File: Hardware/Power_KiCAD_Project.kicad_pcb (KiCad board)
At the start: 4 copper layers, 80 x 93.2 mm, 83 parts, among them J1 Barrel_Jack_MountingPin, J2 XT60 Cell 5, J3 XT60 Cell 4, J4 XT60 Cell 3, J5 XT60 Cell 2, J6 XT60 Cell 1, J7 XT60 To External Switch, J8 L717SDC37P1ACH4F, Q1 PSMN2R6-40YS, Q2 BSS84PH6327XTSA2, Q3 PSMN2R6-40YS, SW1 Reboot, U1 MCP9808_MSOP, U2 MCP9808_MSOP, U3 LM2678SX-5.0/NOPB, U4 LM2678SX-3.3/NOPB, U5 BQ76920PW, U6 STM32L562VET, Y1 32MHz

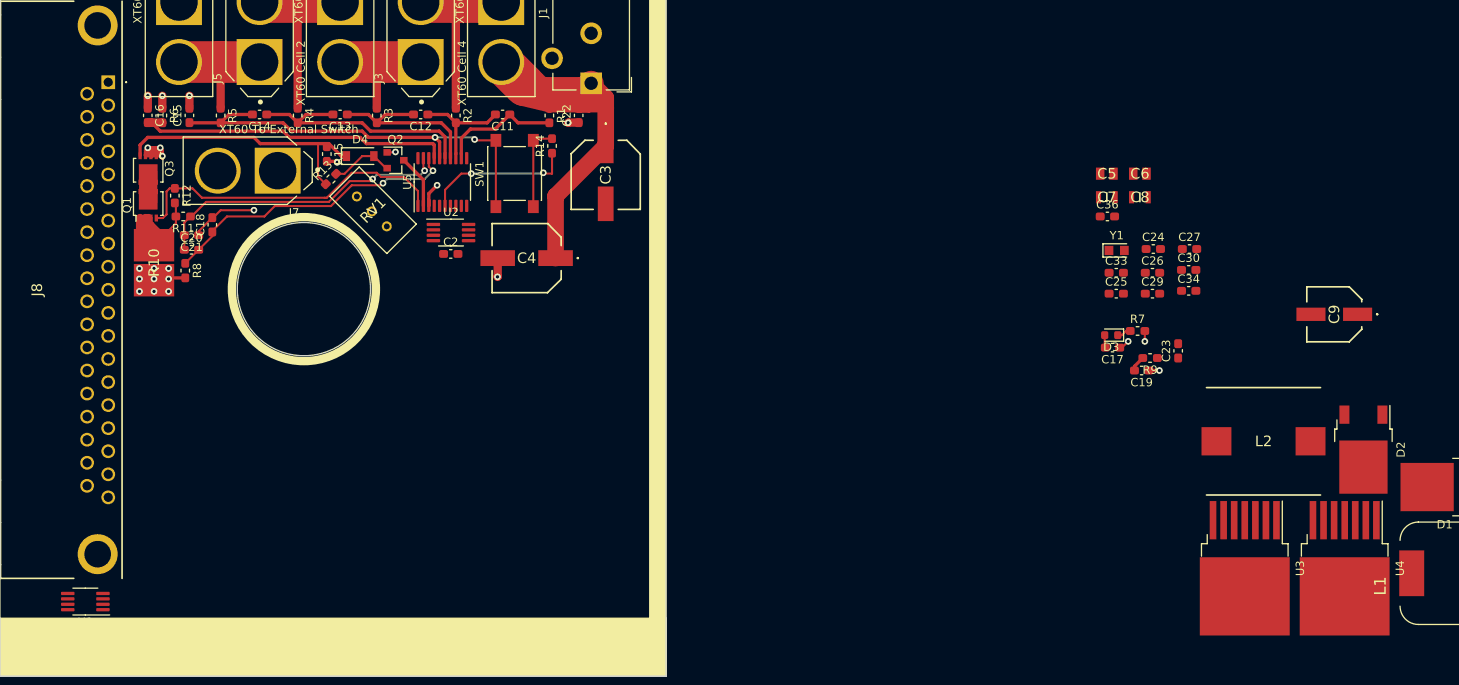
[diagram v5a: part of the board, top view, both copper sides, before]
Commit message: Routed 3v3 and 5v buck converters
Switched to working on my laptop so some of the component references might be messed up for a bit
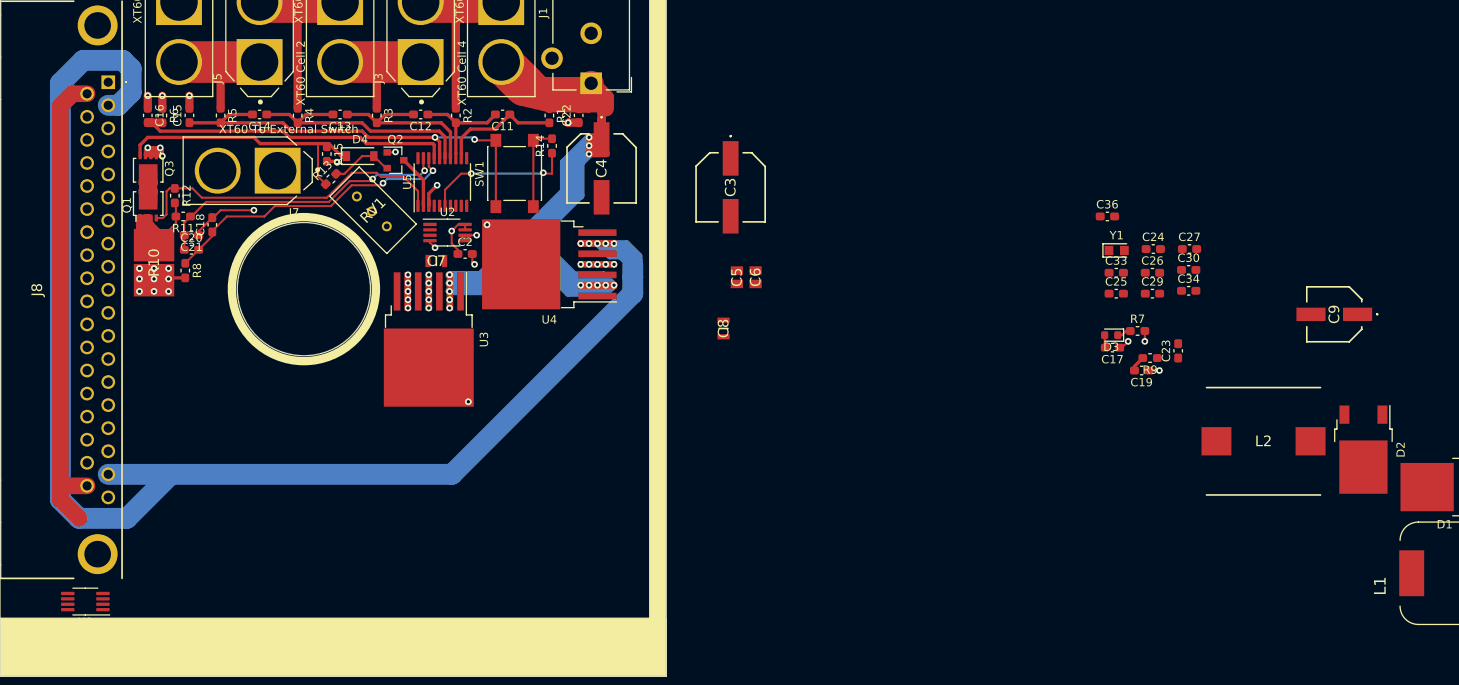
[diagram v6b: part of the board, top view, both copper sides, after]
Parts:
- moved U4 102.3 mm to (146.0, 95.5), turned to 180 degrees
- moved U3 101.8 mm to (131.5, 104.5)
- moved C7 80.9 mm to (132.4, 95.1)
- moved C8 52.4 mm to (166.9, 103.2), turned to 270 degrees
- moved C6 47.8 mm to (170.8, 97.0), turned to 270 degrees
- moved C5 46.1 mm to (168.5, 97.0), turned to 270 degrees
- moved C3 15.1 mm to (167.8, 86.2)
- moved C4 14.0 mm to (152.2, 84.0), turned to 270 degrees
- moved C2 1.73 mm to (135.9, 94.2)
- moved U2 0.42 mm to (133.8, 91.7)
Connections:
- U3 pad 8: (no net) -> GND
- U4 pad 8: (no net) -> GND
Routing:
- net +3V3: track 0.00 -> 190.1 mm, vias 0 -> 6
- net /PACK_M5: track 65.4 -> 182.4 mm, vias 0 -> 13
- net +5V: track 0.00 -> 57.7 mm, vias 0 -> 5
- net GND: track 2.26 -> 4.50 mm, vias 1 -> 15

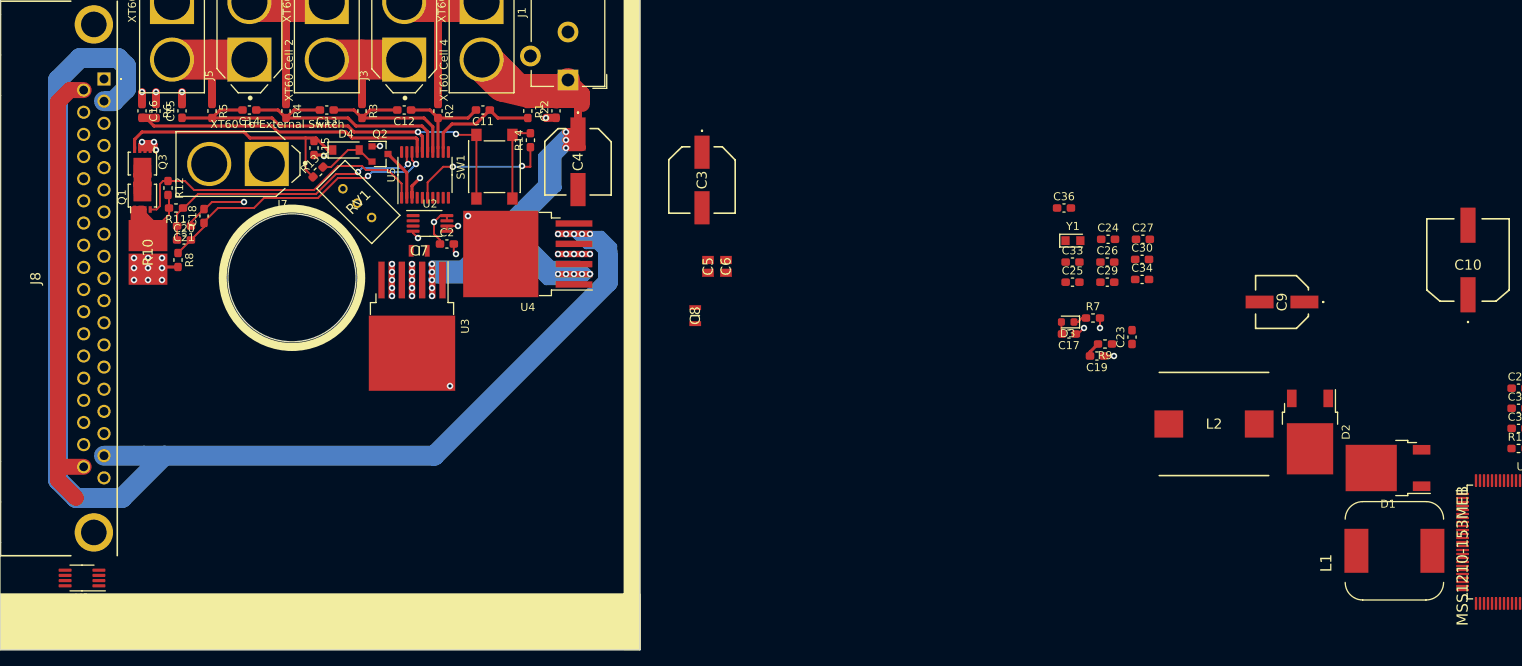
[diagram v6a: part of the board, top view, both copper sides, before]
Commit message: Initial routing and placement of power inductors
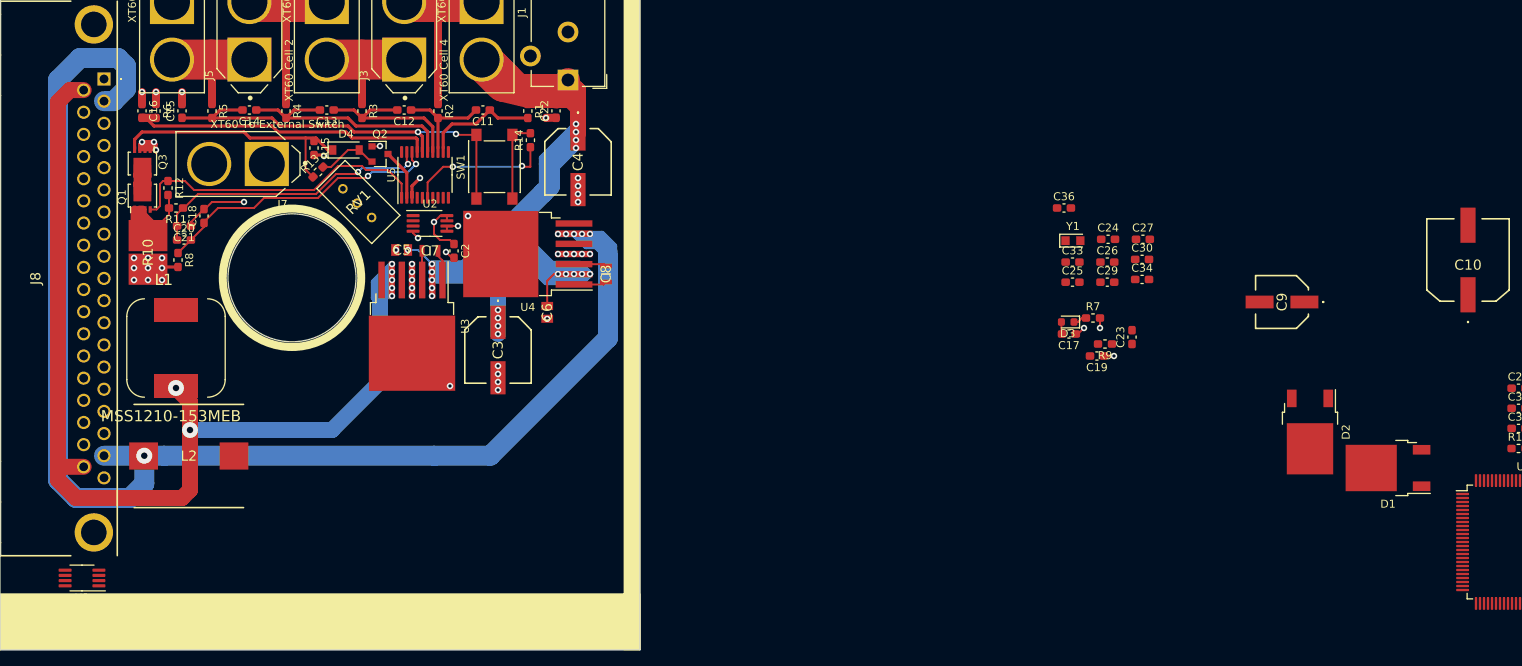
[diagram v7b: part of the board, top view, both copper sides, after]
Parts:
- moved L1 154.4 mm to (102.0, 107.2), turned to 0 degrees
- moved L2 128.2 mm to (103.6, 120.8), turned to 180 degrees
- moved C5 38.4 mm to (130.2, 95.0), turned to 180 degrees
- moved C3 33.2 mm to (142.2, 107.5)
- moved C6 23.1 mm to (148.4, 102.8)
- moved C8 12.3 mm to (155.8, 98.0)
- moved C7 1.35 mm to (133.8, 95.1)
- moved C2 1.24 mm to (136.8, 95.1), turned to 270 degrees
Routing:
- net +5V: track 57.7 -> 138.7 mm, vias 5 -> 7
- net +3V3: track 190.1 -> 195.2 mm, vias 6 -> 7
- net Net-(C8-Pad2): track 0.00 -> 4.13 mm
- net Net-(C8-Pad1): track 0.00 -> 4.10 mm
- net Net-(C7-Pad2): track 0.00 -> 3.88 mm
- net Net-(C7-Pad1): track 0.00 -> 3.66 mm
- net Net-(C19-Pad2): track 1.91 -> 0.00 mm
- net /PACK_M5: track 182.4 -> 180.6 mm, vias 13 -> 19
- net GND: track 4.50 -> 4.44 mm, vias 15 -> 25

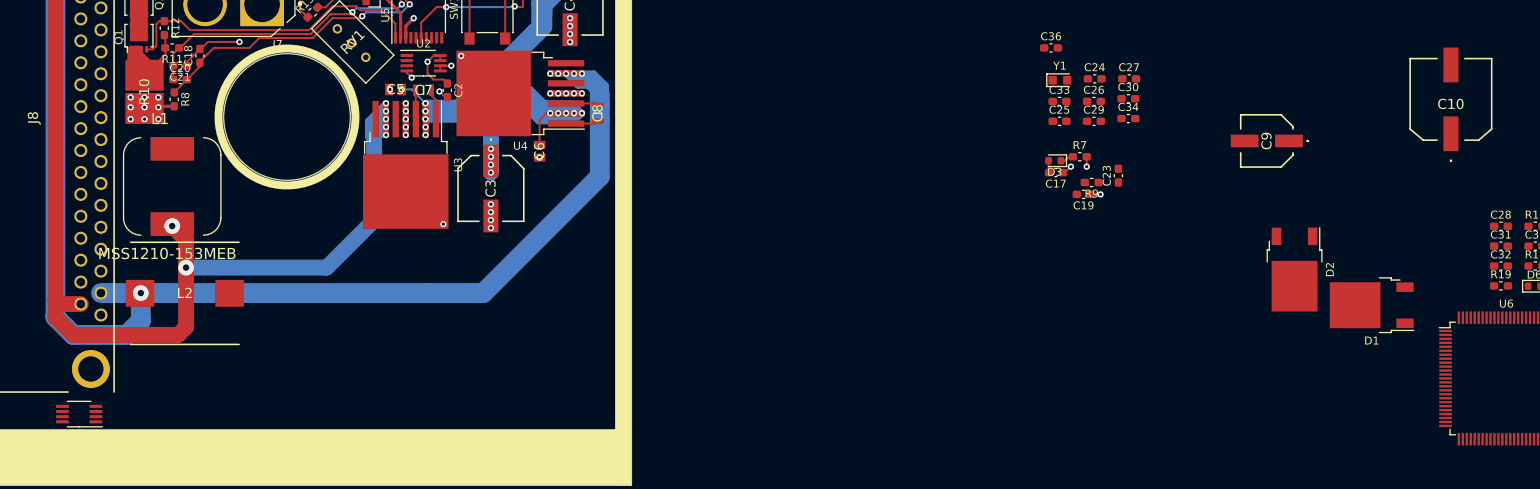
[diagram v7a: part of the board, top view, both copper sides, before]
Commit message: Routed all 3v3 and 5v traces to dsub
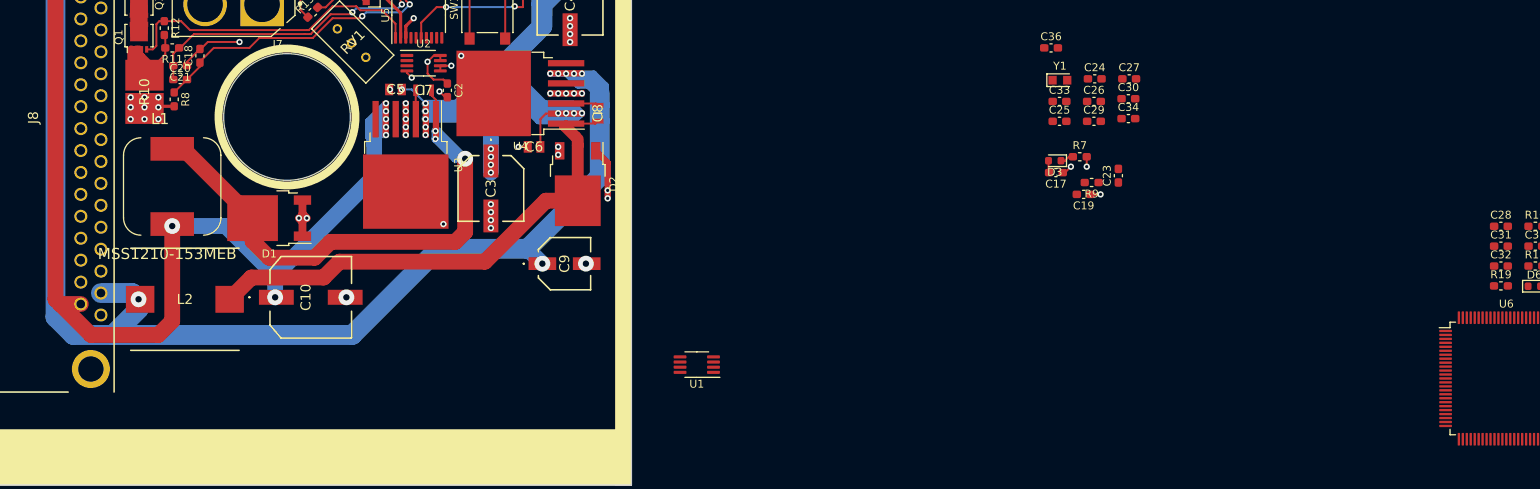
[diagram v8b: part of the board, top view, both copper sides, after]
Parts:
- moved C10 146.2 mm to (119.5, 121.2), turned to 270 degrees
- moved D1 139.7 mm to (114.2, 111.2)
- moved D2 91.2 mm to (153.2, 107.0)
- moved C9 90.0 mm to (151.6, 117.0), turned to 270 degrees
- moved U1 78.2 mm to (168.2, 129.8)
- moved C6 0.89 mm to (147.7, 102.2), turned to 180 degrees
- moved L2 0.75 mm to (103.6, 121.5)
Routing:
- net Net-(C7-Pad2): track 3.88 -> 69.9 mm, vias 0 -> 3
- net Net-(C8-Pad2): track 4.13 -> 67.4 mm
- net GND: track 4.44 -> 17.2 mm, vias 25 -> 33
- net +3V3: track 195.2 -> 201.7 mm, vias 7 -> 8
- net /PACK_M5: track 180.6 -> 182.8 mm, vias 19 -> 18
- net +5V: track 138.7 -> 138.2 mm
